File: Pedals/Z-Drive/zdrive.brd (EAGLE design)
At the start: 55.9 x 54.6 mm, 30 parts, among them IC1 MC1458P, Q1 2N7000, Q2 2N7000

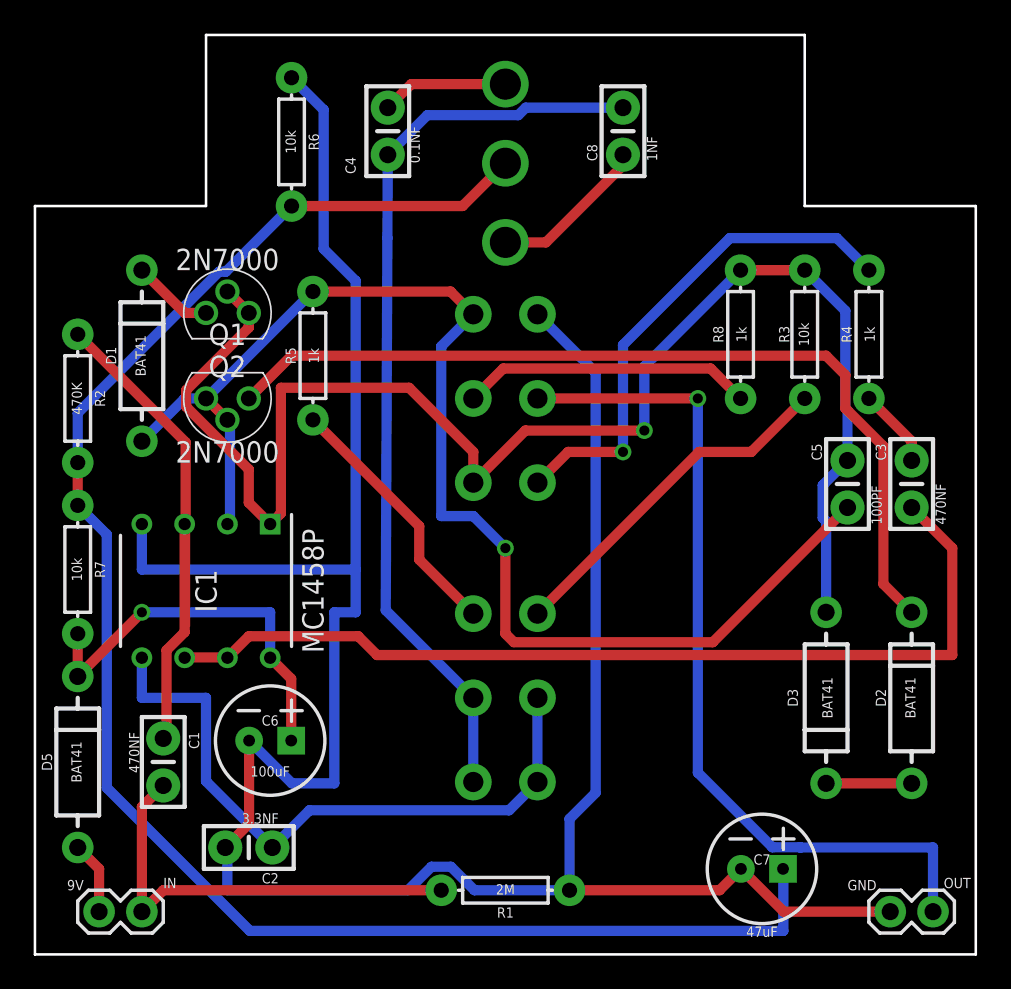
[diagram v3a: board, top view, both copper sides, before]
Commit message: Flip bottom pots
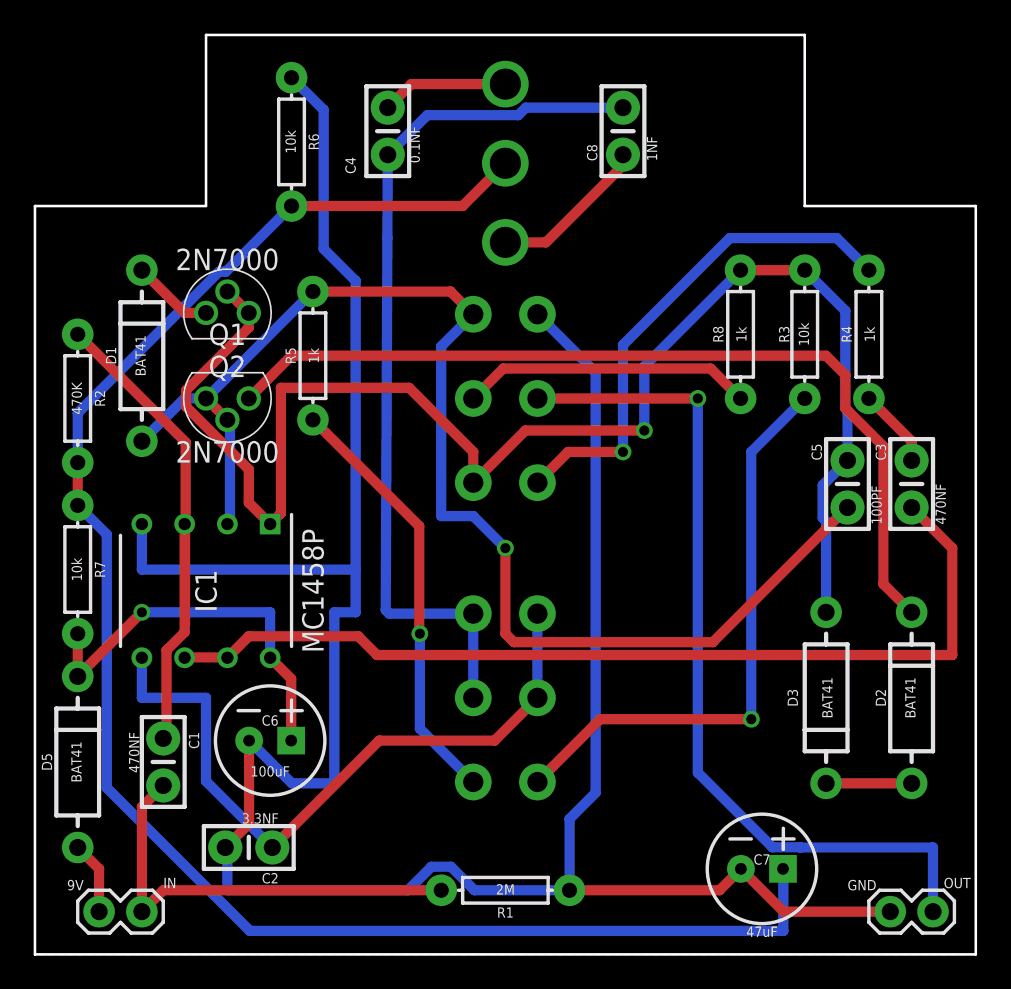
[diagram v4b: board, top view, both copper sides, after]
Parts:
- turned TONE to 90 degrees
- turned VOICE to 270 degrees
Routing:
- net N$1: track 21.2 -> 34.6 mm, vias 0 -> 1
- net N$6: track 15.5 -> 25.5 mm, vias 0 -> 1
- net OP5: track 39.1 -> 41.1 mm
- net N$7: track 54.5 -> 52.5 mm
- added copper zone on layer 1, net GND
- added copper zone on layer 16, net GND
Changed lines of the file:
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@@
 <attribute name="VALUE" x="41.656" y="36.83" size="0.6096" layer="25" font="vector" ratio="20" rot="R90" align="top-center"/>
 </element>
-<element name="TONE" library="Custom-Parts" package="3RP/1610N" package3d_urn="urn:adsk.eagle:package:22726/1" value="B50k" x="29.845" y="15.24" smashed="yes" rot="MR270">
-<attribute name="NAME" x="35.56" y="17.145" size="1.27" layer="26" rot="MR270"/>
-<attribute name="POPULARITY" value="8" x="33.655" y="-30.48" size="1.778" layer="28" rot="MR270" display="off"/>
-<attribute name="VALUE" x="36.195" y="12.7" size="1.27" layer="26" rot="MR90"/>
-</element>
-<element name="VOICE" library="Custom-Parts" package="3RP/1610N" package3d_urn="urn:adsk.eagle:package:22726/1" value="B10k" x="26.035" y="15.24" smashed="yes" rot="MR90">
-<attribute name="NAME" x="20.955" y="12.065" size="1.27" layer="26" rot="MR90"/>
-<attribute name="POPULARITY" value="8" x="9.525" y="36.83" size="1.778" layer="28" rot="MR90" display="off"/>
-<attribute name="VALUE" x="19.05" y="12.7" size="1.27" layer="26" rot="MR90"/>
+<element name="TONE" library="Custom-Parts" package="3RP/1610N" package3d_urn="urn:adsk.eagle:package:22726/1" value="B50k" x="29.845" y="15.24" smashed="yes" rot="MR90">
+<attribute name="NAME" x="31.75" y="12.7" size="1.27" layer="26" rot="MR90"/>
+<attribute name="POPULARITY" value="8" x="26.035" y="60.96" size="1.778" layer="28" rot="MR90" display="off"/>
+<attribute name="VALUE" x="34.925" y="17.145" size="1.27" layer="26" rot="MR270"/>
+</element>
+<element name="VOICE" library="Custom-Parts" package="3RP/1610N" package3d_urn="urn:adsk.eagle:package:22726/1" value="B10k" x="26.035" y="15.24" smashed="yes" rot="MR270">
+<attribute name="NAME" x="24.13" y="17.78" size="1.27" layer="26" rot="MR270"/>
+<attribute name="POPULARITY" value="8" x="42.545" y="-6.35" size="1.778" layer="28" rot="MR270" display="off"/>
+<attribute name="VALUE" x="22.225" y="17.145" size="1.27" layer="26" rot="MR270"/>
 </element>
 <element name="VOL" library="Custom-Parts" package="3RP/1610N" package3d_urn="urn:adsk.eagle:package:22726/1" value="B100k" x="29.845" y="33.02" smashed="yes" rot="MR90">
@@
 <wire x1="33.2994" y1="34.5656" x2="29.845" y2="38.02" width="0.6096" layer="16"/>
 <wire x1="33.2994" y1="9.5982125" x2="33.2994" y2="34.5656" width="0.6096" layer="16"/>
+<polygon width="0.254" layer="16">
+<vertex x="0" y="0"/>
+<vertex x="0" y="44.45"/>
+<vertex x="10.16" y="44.45"/>
+<vertex x="10.16" y="54.61"/>
+<vertex x="45.72" y="54.61"/>
+<vertex x="45.72" y="44.45"/>
+<vertex x="55.88" y="44.45"/>
+<vertex x="55.88" y="0"/>
+</polygon>
+<polygon width="0.254" layer="1">
+<vertex x="0" y="0"/>
+<vertex x="0" y="44.45"/>
+<vertex x="10.16" y="44.45"/>
+<vertex x="10.16" y="54.61"/>
+<vertex x="45.72" y="54.61"/>
+<vertex x="45.72" y="44.45"/>
+<vertex x="55.88" y="44.45"/>
+<vertex x="55.88" y="0"/>
+</polygon>
 </signal>
 <signal name="IN">
@@
 <contactref element="R3" pad="P$2"/>
 <contactref element="TONE" pad="1"/>
-<wire x1="42.545" y1="29.845" x2="39.45" y2="29.845" width="0.6096" layer="1"/>
-<wire x1="42.545" y1="29.845" x2="45.72" y2="33.02" width="0.6096" layer="1"/>
-<wire x1="39.45" y1="29.845" x2="29.845" y2="20.24" width="0.6096" layer="1"/>
+<wire x1="29.845" y1="10.24" x2="33.575" y2="13.97" width="0.6096" layer="1"/>
+<wire x1="33.575" y1="13.97" x2="42.545" y2="13.97" width="0.6096" layer="1"/>
+<via x="42.545" y="13.97" extent="1-16" drill="0.6"/>
+<wire x1="42.545" y1="13.97" x2="42.545" y2="29.845" width="0.6096" layer="16"/>
+<wire x1="42.545" y1="29.845" x2="45.72" y2="33.02" width="0.6096" layer="16"/>
 </signal>
 <signal name="OP5">
@@
 <contactref element="TONE" pad="2"/>
 <contactref element="IC1" pad="5"/>
-<wire x1="29.845" y1="15.24" x2="29.845" y2="10.24" width="0.6096" layer="16"/>
-<wire x1="14.097" y1="6.35" x2="16.3068" y2="8.5598" width="0.6096" layer="16"/>
+<wire x1="29.845" y1="15.24" x2="29.845" y2="20.24" width="0.6096" layer="16"/>
 <wire x1="14.097" y1="6.35" x2="10.16" y2="10.287" width="0.6096" layer="16"/>
 <wire x1="10.16" y1="10.287" x2="10.16" y2="15.24" width="0.6096" layer="16"/>
 <wire x1="10.16" y1="15.24" x2="6.35" y2="15.24" width="0.6096" layer="16"/>
 <wire x1="6.35" y1="15.24" x2="6.35" y2="17.62" width="0.6096" layer="16"/>
-<wire x1="16.3068" y1="8.5598" x2="28.1648" y2="8.5598" width="0.6096" layer="16"/>
-<wire x1="28.1648" y1="8.5598" x2="29.845" y2="10.24" width="0.6096" layer="16"/>
+<wire x1="14.097" y1="6.35" x2="20.447" y2="12.7" width="0.6096" layer="1"/>
+<wire x1="20.447" y1="12.7" x2="27.305" y2="12.7" width="0.6096" layer="1"/>
+<wire x1="27.305" y1="12.7" x2="29.845" y2="15.24" width="0.6096" layer="1"/>
 </signal>
 <signal name="N$2">
@@
 <contactref element="VOICE" pad="3"/>
 <wire x1="16.51" y1="31.75" x2="22.824003125" y2="25.435996875" width="0.6096" layer="1"/>
-<wire x1="22.824003125" y1="25.435996875" x2="22.824003125" y2="23.450996875" width="0.6096" layer="1"/>
-<wire x1="22.824003125" y1="23.450996875" x2="26.035" y2="20.24" width="0.6096" layer="1"/>
+<wire x1="22.824003125" y1="19.085996875" x2="22.86" y2="19.05" width="0.6096" layer="1"/>
+<wire x1="22.824003125" y1="25.435996875" x2="22.824003125" y2="19.085996875" width="0.6096" layer="1"/>
+<via x="22.86" y="19.05" extent="1-16" drill="0.6"/>
+<wire x1="22.86" y1="13.415" x2="26.035" y2="10.24" width="0.6096" layer="16"/>
+<wire x1="22.86" y1="19.05" x2="22.86" y2="13.415" width="0.6096" layer="16"/>
 </signal>
 <signal name="N$7">
@@
 <contactref element="C8" pad="2"/>
 <contactref element="C4" pad="2"/>
-<wire x1="26.035" y1="15.24" x2="26.035" y2="10.24" width="0.6096" layer="16"/>
+<wire x1="26.035" y1="15.24" x2="26.035" y2="20.24" width="0.6096" layer="16"/>
 <wire x1="20.955" y1="47.498" x2="20.932790625" y2="42.5451" width="0.6096" layer="16"/>
 <wire x1="20.932790625" y1="42.5451" x2="20.83366875" y2="20.44133125" width="0.6096" layer="16"/>
-<wire x1="20.83366875" y1="20.44133125" x2="26.035" y2="15.24" width="0.6096" layer="16"/>
 <wire x1="28.7041" y1="49.8453" x2="29.1508" y2="50.292" width="0.6096" layer="16"/>
 <wire x1="29.1508" y1="50.292" x2="34.925" y2="50.292" width="0.6096" layer="16"/>
 <wire x1="23.3023" y1="49.8453" x2="28.7041" y2="49.8453" width="0.6096" layer="16"/>
 <wire x1="20.955" y1="47.498" x2="23.3023" y2="49.8453" width="0.6096" layer="16"/>
+<wire x1="20.83366875" y1="20.44133125" x2="21.035" y2="20.24" width="0.6096" layer="16"/>
+<wire x1="21.035" y1="20.24" x2="26.035" y2="20.24" width="0.6096" layer="16"/>
 </signal>
 <signal name="N$8">
